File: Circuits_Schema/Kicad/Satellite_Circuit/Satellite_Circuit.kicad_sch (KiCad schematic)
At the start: 16 parts, among them IC1 MBED-LPC1768, J1 Conn_01x07, U1 BNO055, U2 ESP32-CAM, U3 DS18B20, Y1 32.768kHZ

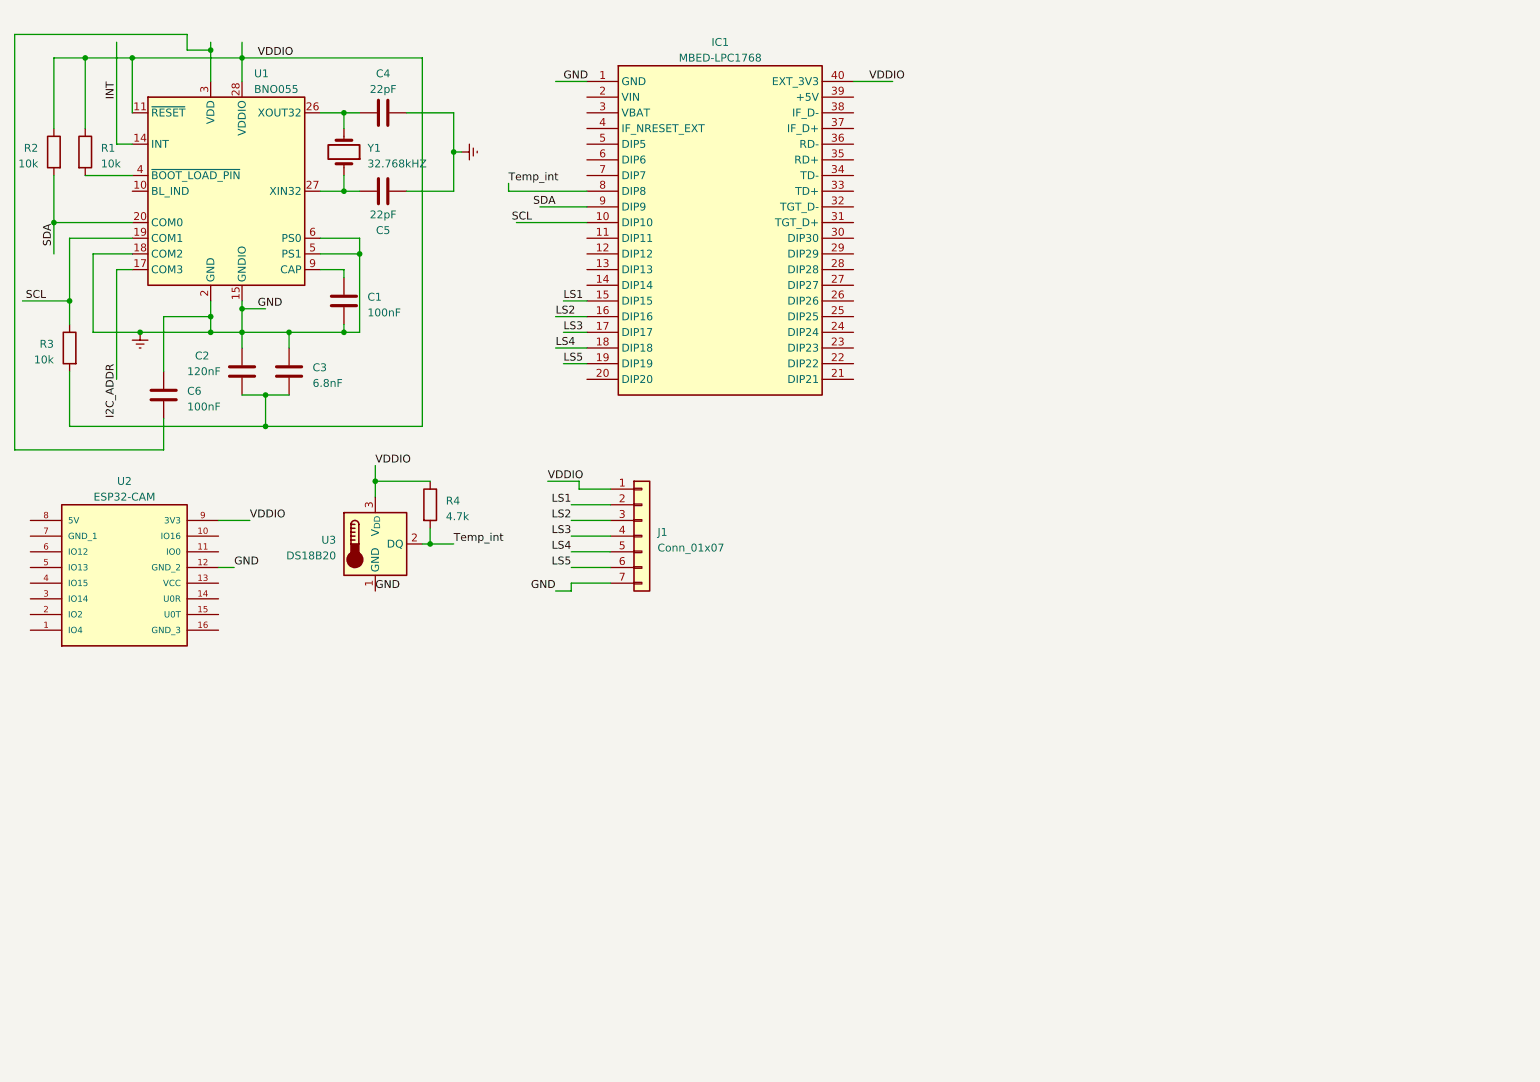
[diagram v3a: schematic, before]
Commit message: MPL3115A2 - Altimeter/Pression sensor added, Labels added
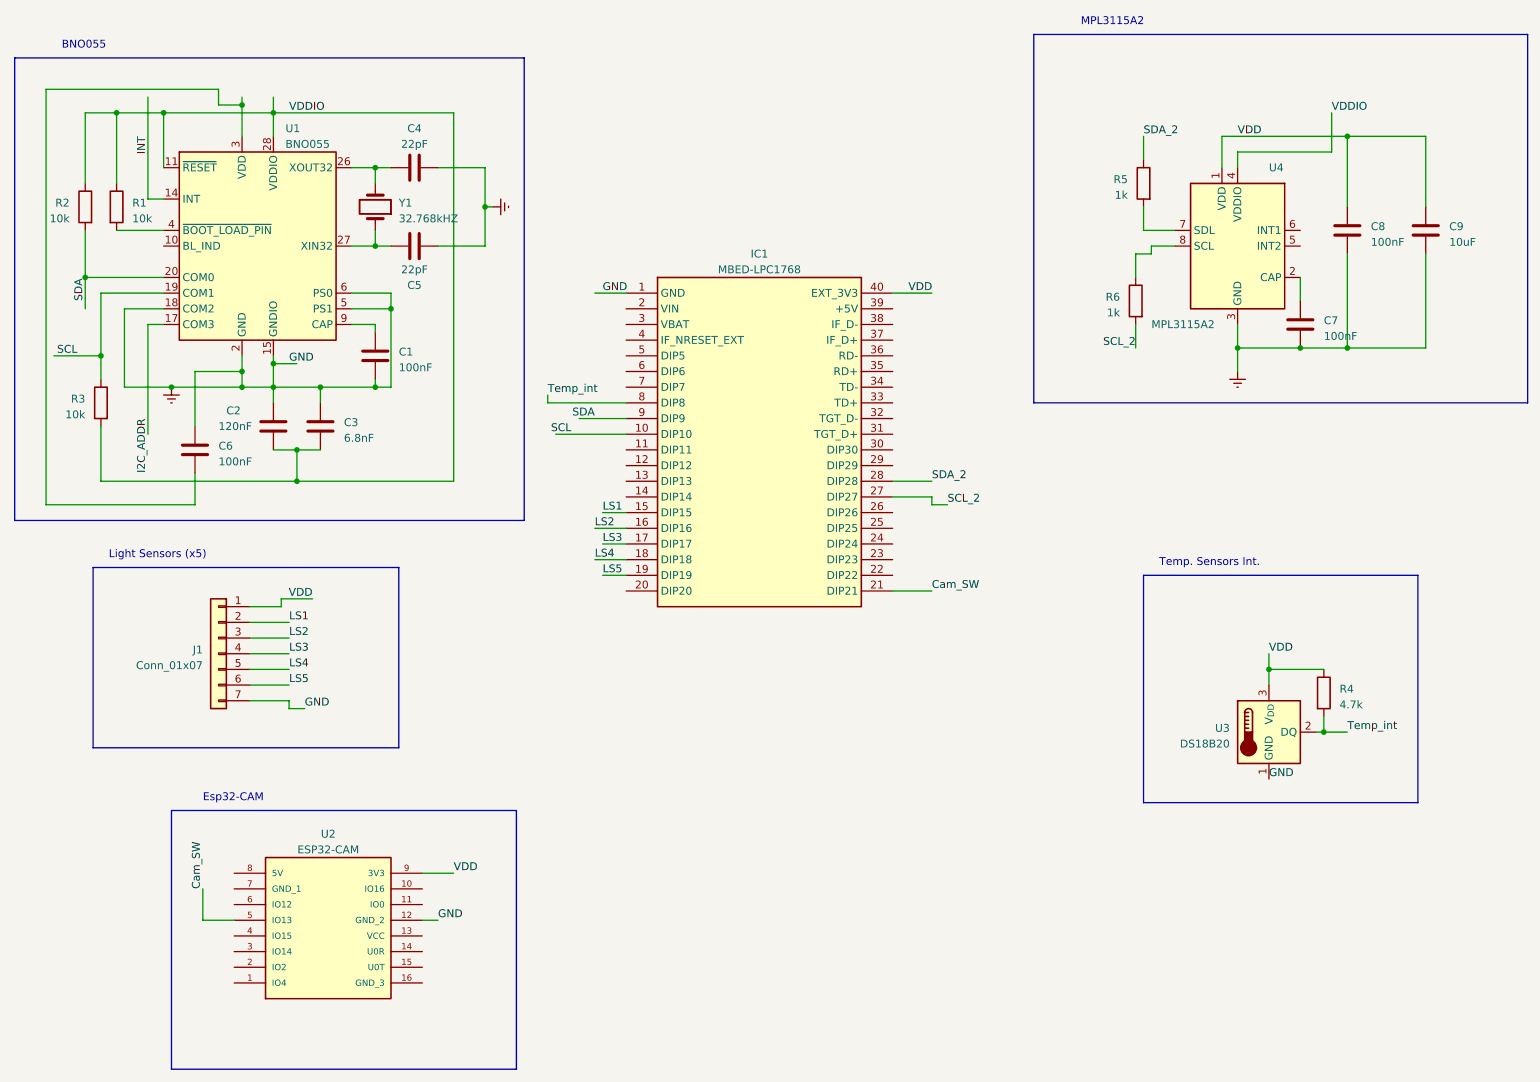
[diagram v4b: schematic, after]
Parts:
- added C7, C8: 100nF, symbol Device:C
- added C9: 10uF, symbol Device:C
- added R5, R6: 1k, symbol Device:R
- added U4: MPL3115A2, Package_LGA:NXP_LGA-8_3x5mm_P1.25mm_H1.1mm, symbol Sensor_Pressure:MPL3115A2
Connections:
- net Earth: now also C7.2, C8.2, C9.2, U4.3 (GND)
- net VDDIO: now also U4.4 (VDDIO); no longer IC1.40 (EXT_3V3), J1.1 (Pin_1), R4.1, U2.9 (3V3), U3.3 (V_{DD})
- net Cam_SW: now reaches IC1.21 (DIP21)
- net Cam_SW: now also U2.5 (IO13)
- net SCL_2: now reaches IC1.27 (DIP27)
- net SCL_2: now also R6.2
- net SDA_2: now reaches IC1.28 (DIP28)
- net SDA_2: now also R5.1
- new net: C7.1, U4.2 (CAP)
- new net: R5.2, U4.7 (SDL)
- new net: R6.1, U4.8 (SCL)
- new net VDD: C8.1, C9.1, IC1.40 (EXT_3V3), J1.1 (Pin_1), R4.1, U2.9 (3V3), U3.3 (V_{DD}), U4.1 (VDD)
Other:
- note added: "BNO055"
- note added: "Esp32-CAM"
- note added: "Light Sensors (x5)"
- note added: "MPL3115A2"
- note added: "Temp. Sensors Int."
- moved on the sheet: C1, C2, C3, C4, C5, C6, IC1, J1, R1, R2, R3, R4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

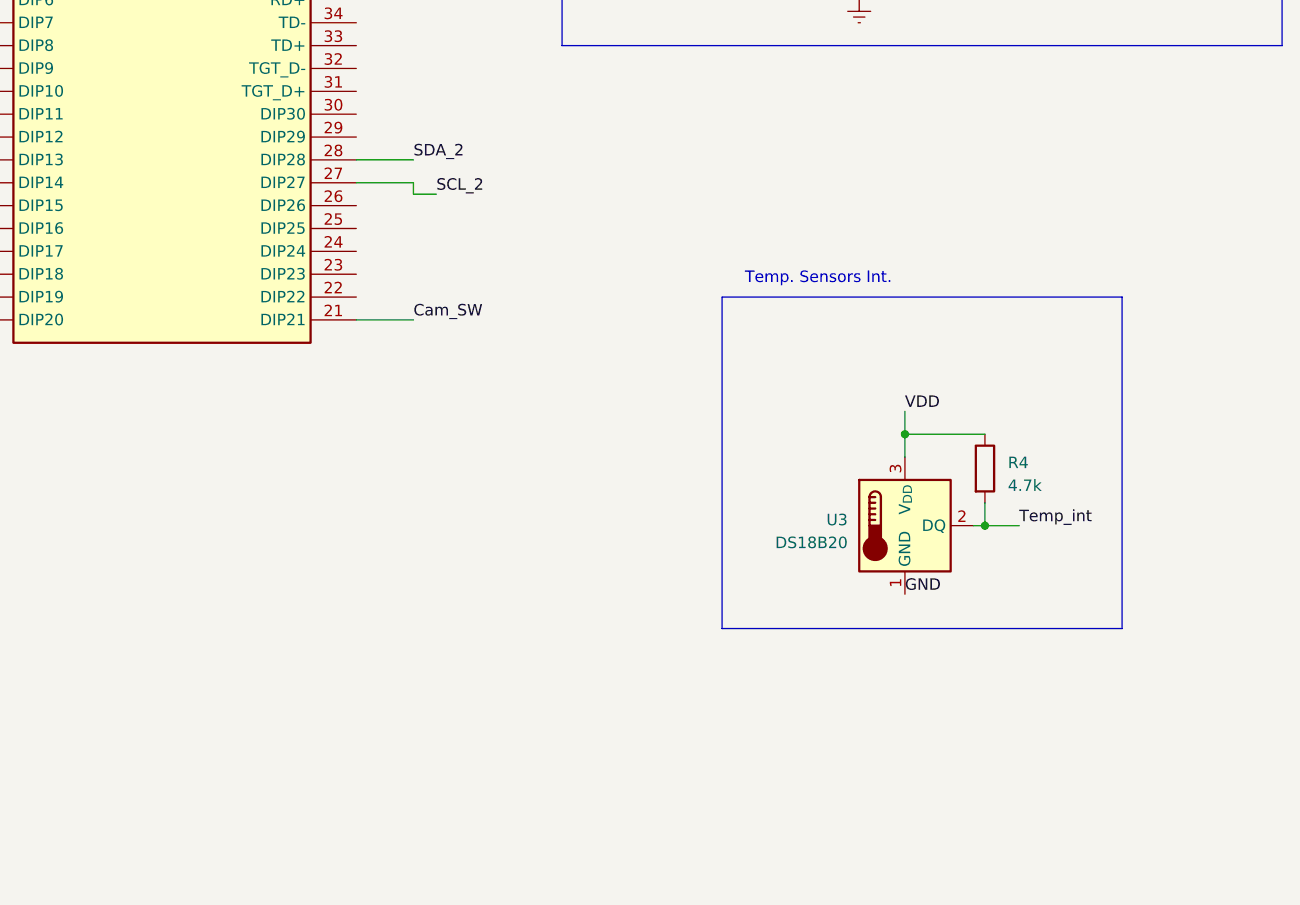
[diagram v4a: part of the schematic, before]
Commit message: Battery added
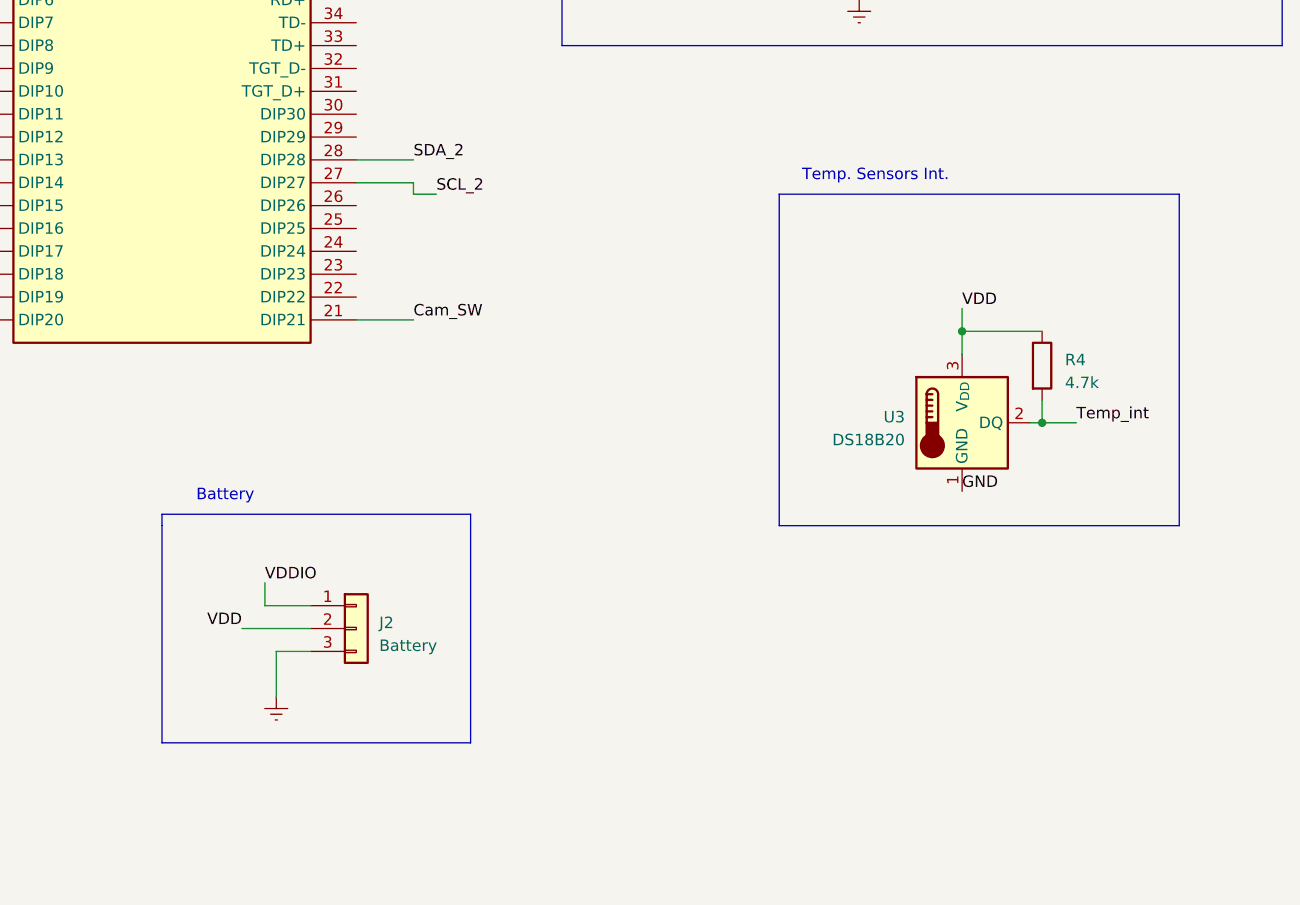
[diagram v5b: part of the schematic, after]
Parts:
- added J2: Battery, symbol Connector_Generic:Conn_01x03
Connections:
- net Earth: now also J2.3 (Pin_3)
- net VDD: now also J2.2 (Pin_2)
- net VDDIO: now also J2.1 (Pin_1)
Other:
- note added: "Battery"
- moved on the sheet: R4, U3
